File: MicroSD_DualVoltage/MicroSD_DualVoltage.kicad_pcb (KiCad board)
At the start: 2 copper layers, 25.4 x 26.7 mm, 21 parts, among them J1 Conn_01x08, U1 AP7365, U2 TXB0104PW

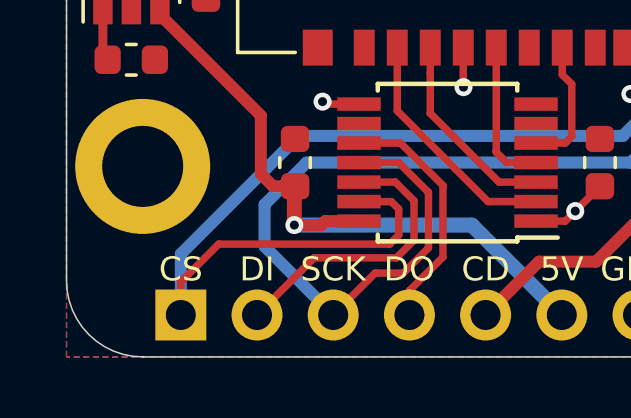
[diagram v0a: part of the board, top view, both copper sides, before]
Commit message: MicroSDv2 Removed and MicroSD and MicroSD_DualVoltage Updated
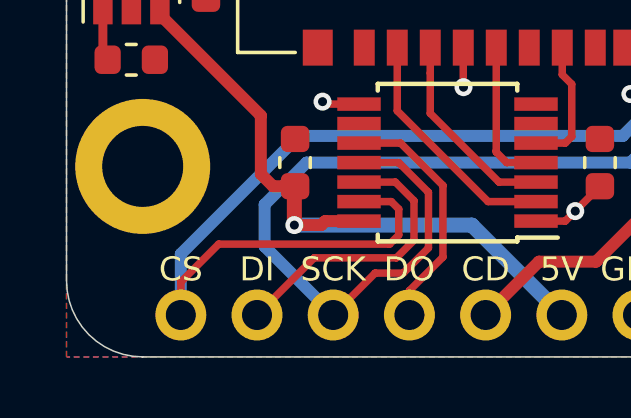
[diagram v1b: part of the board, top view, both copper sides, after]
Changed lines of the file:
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@@
       (effects (font (size 1 1) (thickness 0.15)) (justify mirror))
     )
-    (pad 1 thru_hole rect (at 0 0 270) (size 1.7 1.7) (drill 1) (layers *.Cu *.Mask)
+    (pad 1 thru_hole circle (at 0 0 270) (size 1.7 1.7) (drill 1) (layers *.Cu *.Mask)
       (net 5 CS))
     (pad 2 thru_hole oval (at 0 -2.54 270) (size 1.7 1.7) (drill 1) (layers *.Cu *.Mask)

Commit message: Board Redesign
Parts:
- removed the G*** at (74.5, 28.2)
- removed the G*** at (65.2, 30.9)
- removed the G*** at (65.2, 39.5)
- added G***: LOGO, logo:SirBoard112x35, B.Cu at (67.4, 35.7)
- added G***: LOGO, logo:logo76x107, B.Cu at (67.4, 29.7)
- added R4: 10K, Resistor_SMD:R_0603_1608Metric, F.Cu at (77.5, 30.9)
- C1, C2: value 1uF -> 10uF; footprint Capacitor_SMD:C_0603_1608Metric -> Capacitor_SMD:C_0805_2012Metric
- H1, H2, H3, H4: footprint MountingHole:MountingHole_2.7mm_M2.5_ISO14580_Pad -> SirBoardLibrary:MountingHole_M2.5_SirBoard
- J3: renamed from HIROSE DM3AT
- R2: value 12K5 -> 12K4
- moved H3 29.6 mm to (54.9, 43.3), turned to 0 degrees
- moved H2 27.8 mm to (80.3, 28.1), turned to 0 degrees
- moved C1 27.2 mm to (81.7, 39.2), turned to 90 degrees
- moved JP1 26.5 mm to (80.8, 34.2), turned to 270 degrees
- moved U1 25.0 mm to (78.9, 39.2), turned to 180 degrees
- moved R2 24.6 mm to (77.5, 35.8), turned to 0 degrees
- moved C2 22.9 mm to (76.1, 39.2)
- moved R1 20.7 mm to (77.5, 32.5), turned to 0 degrees
- moved R3 20.4 mm to (77.5, 34.2), turned to 180 degrees
- moved R6 19.6 mm to (54.7, 39.8), turned to 0 degrees
- moved D1 18.4 mm to (57.9, 39.8), turned to 180 degrees
- moved C4 13.1 mm to (59.3, 32.4), turned to 270 degrees
- moved U2 10.9 mm to (55.5, 34.5), turned to 270 degrees
- moved J3 6.48 mm to (67.6, 34.1)
- moved H1 6.10 mm to (54.9, 28.1), turned to 0 degrees
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- renumbered STAT to D1
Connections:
- J3 pad 9: DETB -> VOUT
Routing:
- net CS: track 36.0 -> 8.18 mm, vias 1 -> 0
- net /DO_SD: track 4.38 -> 27.2 mm, vias 0 -> 2
- net /CLK_SD: track 4.95 -> 24.0 mm, vias 0 -> 2
- net /DI_SD: track 6.66 -> 20.8 mm, vias 0 -> 2
- net DO: track 8.16 -> 20.9 mm, vias 0 -> 1
- net /CS_SD: track 7.98 -> 18.7 mm, vias 0 -> 2
- net SCK: track 31.2 -> 20.6 mm
- net VOUT: track 10.1 -> 18.2 mm
- net DETA: track 25.0 -> 18.5 mm, vias 2 -> 1
- net VIN: track 27.4 -> 33.7 mm
- net DI: track 9.67 -> 14.3 mm, vias 0 -> 1
- net ADJ: track 10.6 -> 7.41 mm, vias 2 -> 0
- net Net-(JP1-Pad3): track 2.15 -> 2.66 mm
- net Net-(JP1-Pad1): track 2.15 -> 2.66 mm
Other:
- board size 25.4 x 26.7 mm -> 30.5 x 20.3 mm
- board text added: "DETA"
- board text added: "MicroSD to DIP Breakout With TXB0104 Level-Shift"
- board text removed: "CD"
- board text removed: "MicroSD Breakout TXB0104 Level Shift 1.8V AND 3.3V SD"

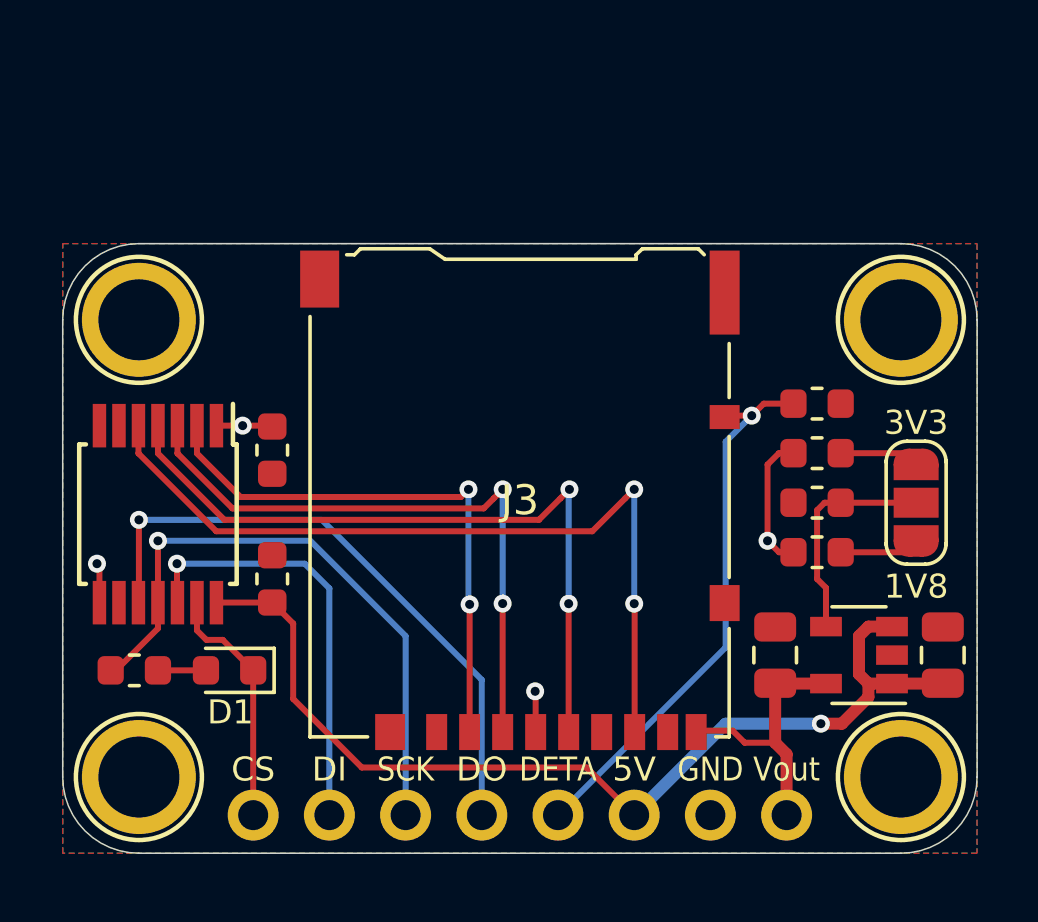
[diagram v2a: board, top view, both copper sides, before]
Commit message: Breakout Boards Revision 2
Renders updated, silkscreen text improved, blurry silkscreen items removed/resized.
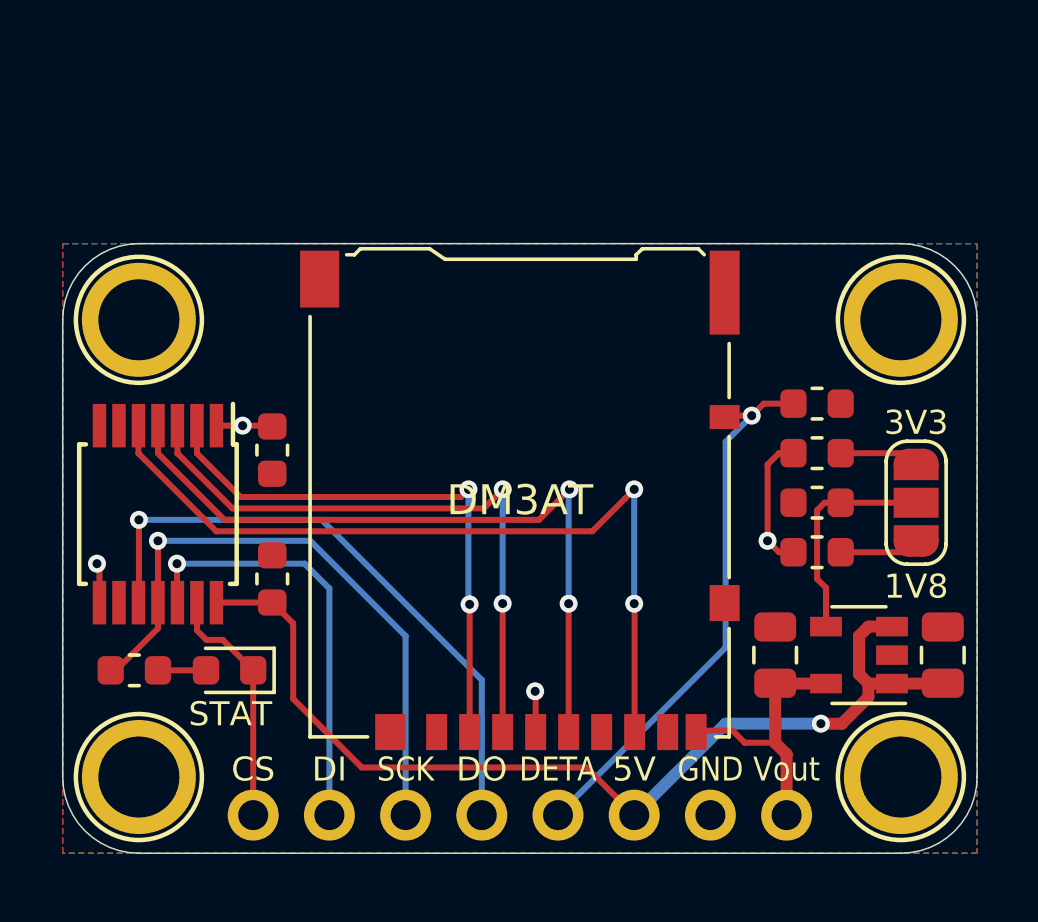
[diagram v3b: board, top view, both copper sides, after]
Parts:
- G***: footprint logo:SirBoard112x35 -> logo:SirBoard127x40
- moved G*** 0.19 mm to (67.4, 35.9)
- renumbered J3 to DM3AT, D1 to STAT
